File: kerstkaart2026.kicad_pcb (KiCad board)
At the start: 2 copper layers, 96 x 99.4 mm, 58 parts, among them J1 UPDI 1x3, J2 BT+ BT-, J3 SCHAKELAAR, SW1 Tact SMD, U1 ATtiny1616-SU (SOIC-20)

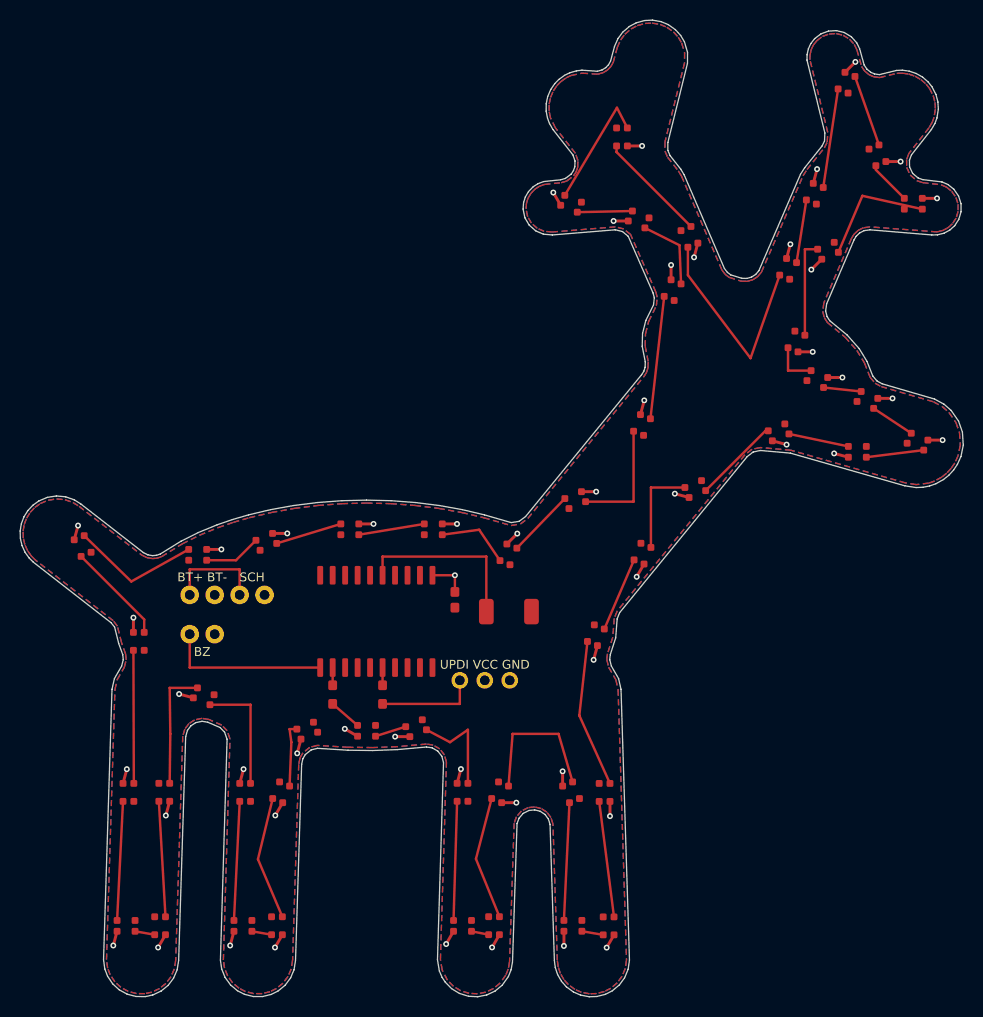
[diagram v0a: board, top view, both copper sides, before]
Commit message: Kerstkaart 2026 v2: echte footprints, QFN, achterpads (UPDI direct + 4k7), knop, symmetrische geweien, boodschap, Gerbers/BOM/CPL
Co-Authored-By: Claude Sonnet 5.5 <noreply@anthropic.com>
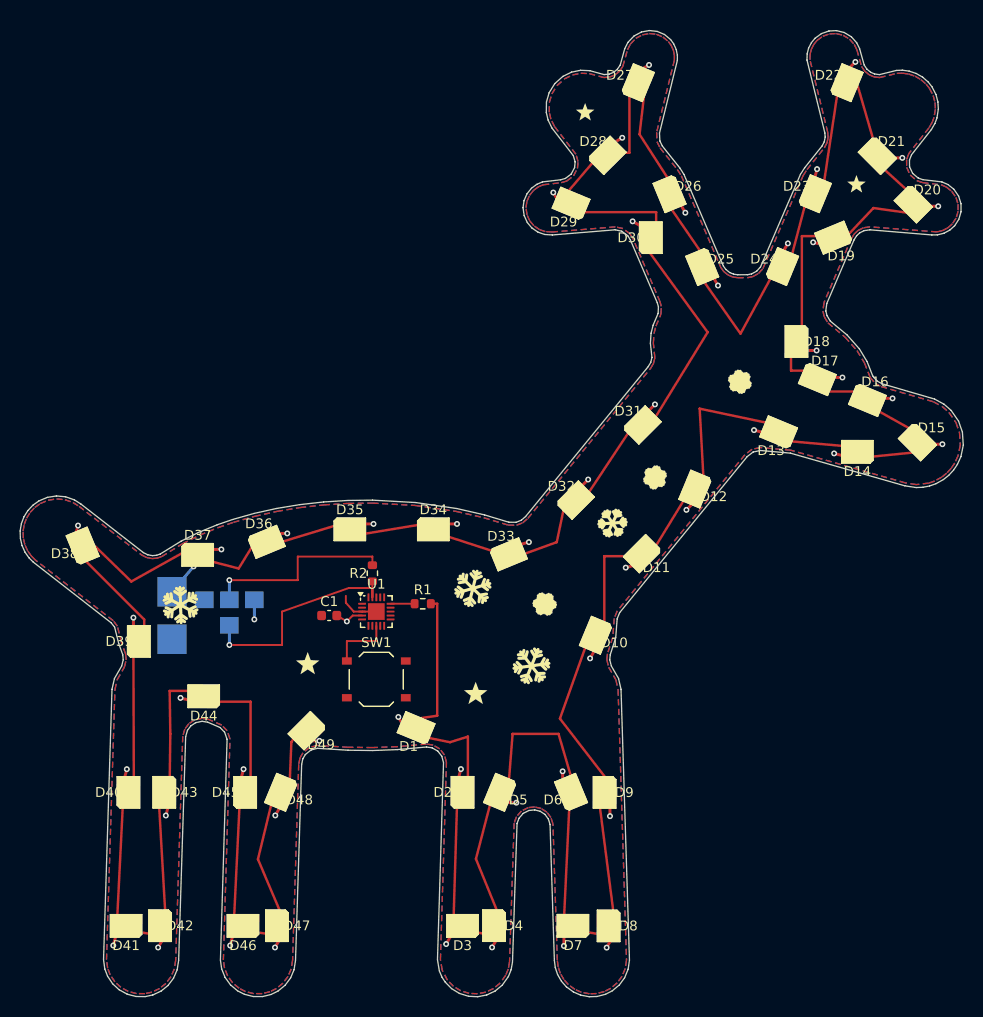
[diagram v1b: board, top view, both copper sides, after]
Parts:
- removed BZ1: BUZZER, kerstkaart:BZ1
- removed J1: UPDI 1x3, kerstkaart:J1
- removed J2: BT+ BT-, kerstkaart:J2
- removed J3: SCHAKELAAR, kerstkaart:J3
- added TP_BT+: , kerstkaart:Pad_BT+, B.Cu at (34.2, 104.0)
- added TP_BT-: , kerstkaart:Pad_BT-, B.Cu at (34.2, 99.2)
- added TP_GND: , kerstkaart:Pad_GND, B.Cu at (42.6, 100.0)
- added TP_HV: , kerstkaart:Pad_HV, B.Cu at (40.0, 102.6)
- added TP_UPDI: , kerstkaart:Pad_UPDI, B.Cu at (40.0, 100.0)
- added TP_VCC: , kerstkaart:Pad_VCC, B.Cu at (37.5, 100.0)
- C1: footprint kerstkaart:C1 -> kerstkaart:C_0603_1608Metric
- D1: footprint kerstkaart:D1 -> kerstkaart:LED_WS2812B-2020_PLCC4_2.0x2.0mm
- D10: footprint kerstkaart:D10 -> kerstkaart:LED_WS2812B-2020_PLCC4_2.0x2.0mm
- D11: footprint kerstkaart:D11 -> kerstkaart:LED_WS2812B-2020_PLCC4_2.0x2.0mm
- D12: footprint kerstkaart:D12 -> kerstkaart:LED_WS2812B-2020_PLCC4_2.0x2.0mm
- D13: footprint kerstkaart:D13 -> kerstkaart:LED_WS2812B-2020_PLCC4_2.0x2.0mm
- D14: footprint kerstkaart:D14 -> kerstkaart:LED_WS2812B-2020_PLCC4_2.0x2.0mm
- D15: footprint kerstkaart:D15 -> kerstkaart:LED_WS2812B-2020_PLCC4_2.0x2.0mm
- D16: footprint kerstkaart:D16 -> kerstkaart:LED_WS2812B-2020_PLCC4_2.0x2.0mm
- D17: footprint kerstkaart:D17 -> kerstkaart:LED_WS2812B-2020_PLCC4_2.0x2.0mm
- D18: footprint kerstkaart:D18 -> kerstkaart:LED_WS2812B-2020_PLCC4_2.0x2.0mm
- D19: footprint kerstkaart:D19 -> kerstkaart:LED_WS2812B-2020_PLCC4_2.0x2.0mm
- D2: footprint kerstkaart:D2 -> kerstkaart:LED_WS2812B-2020_PLCC4_2.0x2.0mm
- D20: footprint kerstkaart:D20 -> kerstkaart:LED_WS2812B-2020_PLCC4_2.0x2.0mm
- D21: footprint kerstkaart:D21 -> kerstkaart:LED_WS2812B-2020_PLCC4_2.0x2.0mm
- D22: footprint kerstkaart:D22 -> kerstkaart:LED_WS2812B-2020_PLCC4_2.0x2.0mm
- D23: footprint kerstkaart:D23 -> kerstkaart:LED_WS2812B-2020_PLCC4_2.0x2.0mm
- D24: footprint kerstkaart:D24 -> kerstkaart:LED_WS2812B-2020_PLCC4_2.0x2.0mm
- D25: footprint kerstkaart:D25 -> kerstkaart:LED_WS2812B-2020_PLCC4_2.0x2.0mm
- D26: footprint kerstkaart:D26 -> kerstkaart:LED_WS2812B-2020_PLCC4_2.0x2.0mm
- D27: footprint kerstkaart:D27 -> kerstkaart:LED_WS2812B-2020_PLCC4_2.0x2.0mm
- D28: footprint kerstkaart:D28 -> kerstkaart:LED_WS2812B-2020_PLCC4_2.0x2.0mm
- D29: footprint kerstkaart:D29 -> kerstkaart:LED_WS2812B-2020_PLCC4_2.0x2.0mm
- D3: footprint kerstkaart:D3 -> kerstkaart:LED_WS2812B-2020_PLCC4_2.0x2.0mm
- D30: footprint kerstkaart:D30 -> kerstkaart:LED_WS2812B-2020_PLCC4_2.0x2.0mm
- D31: footprint kerstkaart:D31 -> kerstkaart:LED_WS2812B-2020_PLCC4_2.0x2.0mm
- D32: footprint kerstkaart:D32 -> kerstkaart:LED_WS2812B-2020_PLCC4_2.0x2.0mm
- D33: footprint kerstkaart:D33 -> kerstkaart:LED_WS2812B-2020_PLCC4_2.0x2.0mm
- D34: footprint kerstkaart:D34 -> kerstkaart:LED_WS2812B-2020_PLCC4_2.0x2.0mm
- D35: footprint kerstkaart:D35 -> kerstkaart:LED_WS2812B-2020_PLCC4_2.0x2.0mm
- D36: footprint kerstkaart:D36 -> kerstkaart:LED_WS2812B-2020_PLCC4_2.0x2.0mm
- D37: footprint kerstkaart:D37 -> kerstkaart:LED_WS2812B-2020_PLCC4_2.0x2.0mm
- D38: footprint kerstkaart:D38 -> kerstkaart:LED_WS2812B-2020_PLCC4_2.0x2.0mm
- D39: footprint kerstkaart:D39 -> kerstkaart:LED_WS2812B-2020_PLCC4_2.0x2.0mm
- D4: footprint kerstkaart:D4 -> kerstkaart:LED_WS2812B-2020_PLCC4_2.0x2.0mm
- D40: footprint kerstkaart:D40 -> kerstkaart:LED_WS2812B-2020_PLCC4_2.0x2.0mm
- D41: footprint kerstkaart:D41 -> kerstkaart:LED_WS2812B-2020_PLCC4_2.0x2.0mm
- D42: footprint kerstkaart:D42 -> kerstkaart:LED_WS2812B-2020_PLCC4_2.0x2.0mm
- D43: footprint kerstkaart:D43 -> kerstkaart:LED_WS2812B-2020_PLCC4_2.0x2.0mm
- D44: footprint kerstkaart:D44 -> kerstkaart:LED_WS2812B-2020_PLCC4_2.0x2.0mm
- D45: footprint kerstkaart:D45 -> kerstkaart:LED_WS2812B-2020_PLCC4_2.0x2.0mm
- D46: footprint kerstkaart:D46 -> kerstkaart:LED_WS2812B-2020_PLCC4_2.0x2.0mm
- D47: footprint kerstkaart:D47 -> kerstkaart:LED_WS2812B-2020_PLCC4_2.0x2.0mm
- D48: footprint kerstkaart:D48 -> kerstkaart:LED_WS2812B-2020_PLCC4_2.0x2.0mm
- D49: footprint kerstkaart:D49 -> kerstkaart:LED_WS2812B-2020_PLCC4_2.0x2.0mm
- D5: footprint kerstkaart:D5 -> kerstkaart:LED_WS2812B-2020_PLCC4_2.0x2.0mm
- D6: footprint kerstkaart:D6 -> kerstkaart:LED_WS2812B-2020_PLCC4_2.0x2.0mm
- D7: footprint kerstkaart:D7 -> kerstkaart:LED_WS2812B-2020_PLCC4_2.0x2.0mm
- D8: footprint kerstkaart:D8 -> kerstkaart:LED_WS2812B-2020_PLCC4_2.0x2.0mm
- D9: footprint kerstkaart:D9 -> kerstkaart:LED_WS2812B-2020_PLCC4_2.0x2.0mm
- R1: footprint kerstkaart:R1 -> kerstkaart:R_0603_1608Metric
- R2: value 470R 0603 -> 4.7k 0603; footprint kerstkaart:R2 -> kerstkaart:R_0603_1608Metric
- SW1: value Tact SMD -> TS-1187A-B-A-B; footprint kerstkaart:SW1 -> kerstkaart:SW_Push_1P1T_XKB_TS-1187A
- U1: value ATtiny1616-SU (SOIC-20) -> ATtiny1616-MNR (VQFN-20); footprint kerstkaart:U1 -> kerstkaart:VQFN-20-1EP_3x3mm_P0.4mm_EP1.7x1.7mm
- moved D10 16.0 mm to (77.4, 103.6), turned to 247.5 degrees
- moved SW1 15.2 mm to (55.0, 108.1)
- moved D3 13.6 mm to (63.8, 133.2), turned to 180 degrees
- moved D7 13.6 mm to (75.0, 133.2), turned to 180 degrees
- moved D5 13.6 mm to (67.6, 119.6), turned to 247.5 degrees
- moved D9 13.6 mm to (78.2, 119.6), turned to 270 degrees
- moved R1 13.0 mm to (59.7, 100.4)
- moved C1 12.9 mm to (50.2, 101.6)
- moved R2 12.4 mm to (54.6, 97.3), turned to 90 degrees
- moved D23 11.8 mm to (99.6, 58.7), turned to 67.5 degrees
- moved D19 11.2 mm to (101.6, 63.1), turned to 202.5 degrees
- moved D13 10.3 mm to (96.0, 83.0), turned to 157.5 degrees
- moved D20 9.92 mm to (109.7, 59.7), turned to 315 degrees
- moved D11 9.57 mm to (82.1, 95.3), turned to 225 degrees
- moved D25 8.75 mm to (88.2, 66.1), turned to 292.5 degrees
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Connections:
- C1 pad 1: VCC -> GND
- C1 pad 2: GND -> VCC
- R2 pad 2: UPDI -> UPDI_R
- U1 pad 1: VCC -> (no net)
- U1 pad 11: BUZ -> (no net)
- U1 pad 12: DATA0 -> (no net)
- U1 pad 15: (no net) -> DATA0
- U1 pad 16: UPDI0 -> (no net)
- U1 pad 19: (no net) -> UPDI0
- U1 pad 20: GND -> (no net)
- U1 pad 3: (no net) -> GND
- U1 pad 4: (no net) -> VCC
- U1 pad 5: BTN -> (no net)
- U1 pad 8: (no net) -> BTN
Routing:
- net UPDI0: track 1.80 -> 22.9 mm, vias 0 -> 1
- net UPDI_R: track 0.00 -> 19.8 mm, vias 0 -> 1
- net BUZ: track 16.7 -> 0.00 mm
- net D25: track 22.4 -> 6.43 mm
- net DATA1: track 3.35 -> 14.9 mm
- net D4: track 1.78 -> 12.7 mm
- net BTN: track 17.1 -> 6.57 mm
- net D3: track 12.1 -> 1.78 mm
- net VBAT: track 10.3 -> 0.00 mm
- net UPDI: track 10.3 -> 0.00 mm
- net D7: track 12.0 -> 2.20 mm
- net D8: track 2.20 -> 11.9 mm
- net GND: track 0.00 -> 9.11 mm, vias 0 -> 2
- net D30: track 12.5 -> 21.6 mm
- net D20: track 12.5 -> 4.25 mm
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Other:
- board size 96 x 99.4 mm -> 96 x 98.4 mm
- board text removed: "BT+ BT-"
- board text removed: "BZ"
- board text removed: "Kerstkaart 2026"
- board text removed: "SCH"
- board text removed: "UPDI VCC GND"
